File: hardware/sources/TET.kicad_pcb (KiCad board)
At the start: 4 copper layers, 90.2 x 95.9 mm, 97 parts, among them J1 SWD, M1 MountingHole, M2 MountingHole, M3 MountingHole, M4 MountingHole, U1 TCAN330GDCNR, U10 TLV75533PDBVR, U11 SMA_1, U12 W25Q128JVSIQTR, U13 W25Q128JVSIQTR, U14 E80-900M2213S, U15 SMA_2, U16 W25Q128JVSIQTR, U17 TMP112AIDRLR, U18 INA226AQDGSRQ1, U19 TMP112AIDRLR, U2 8 MHz, U3 STM32L431RBT6TR, U4 TMP112AIDRLR, U6 5015, U7 5015, U8 INA226AQDGSRQ1, U9 TMP112AIDRLR

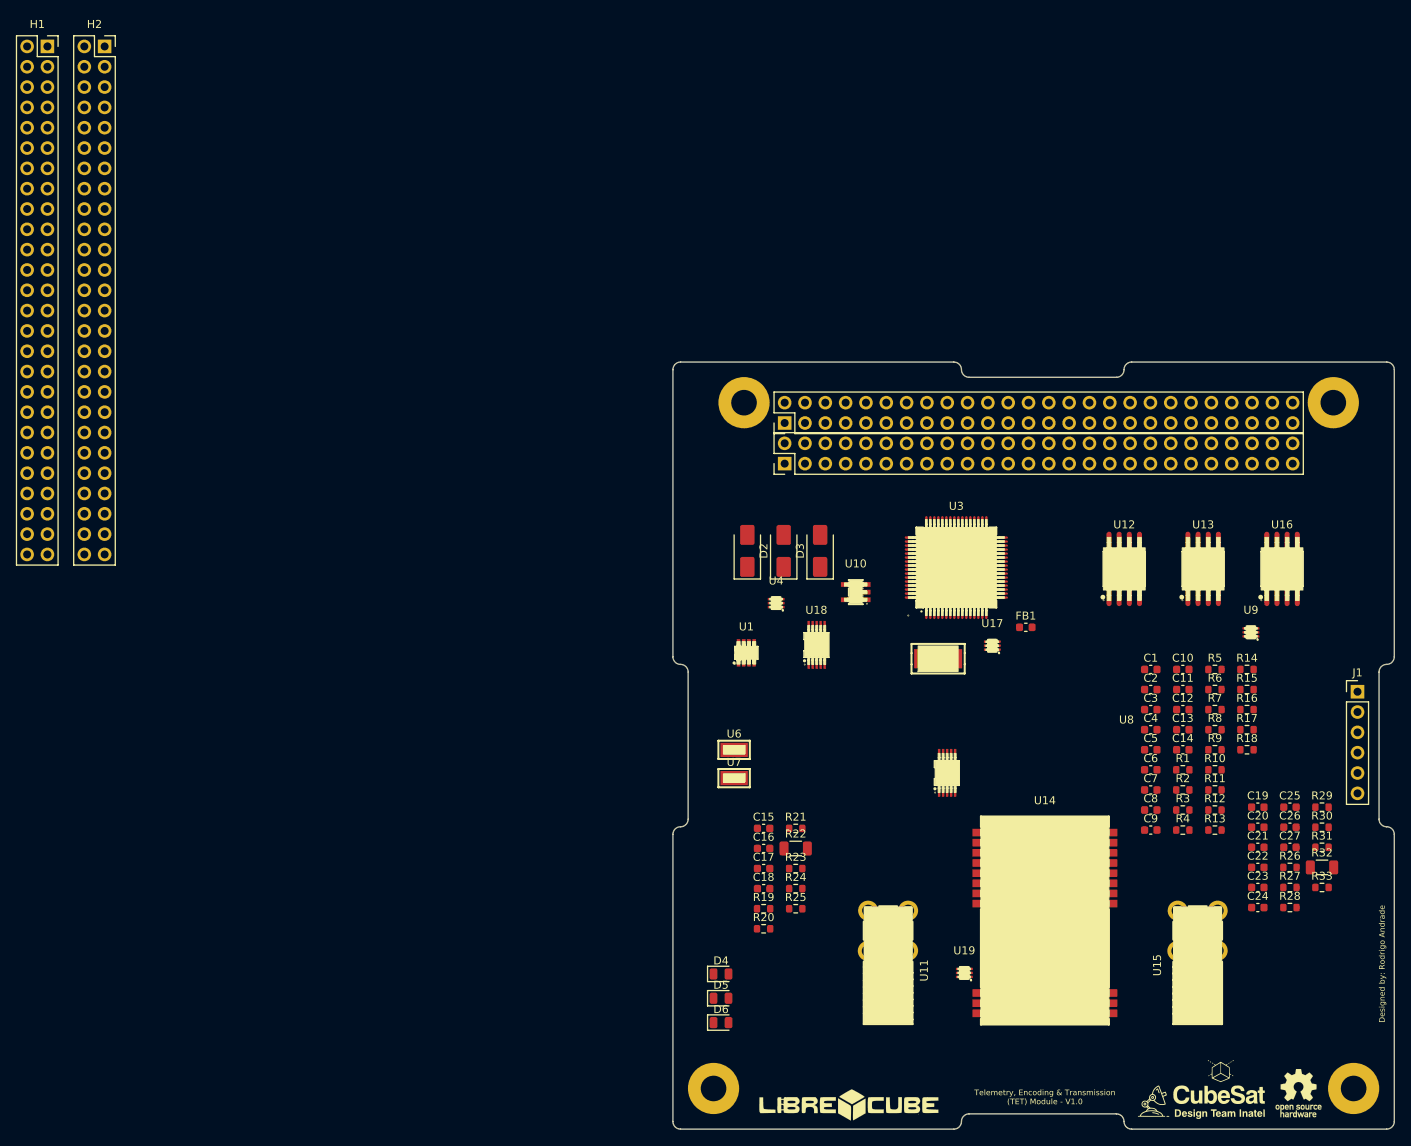
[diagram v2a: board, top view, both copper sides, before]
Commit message: hardware(schematic): fix Electrical Rules Check (ERC)
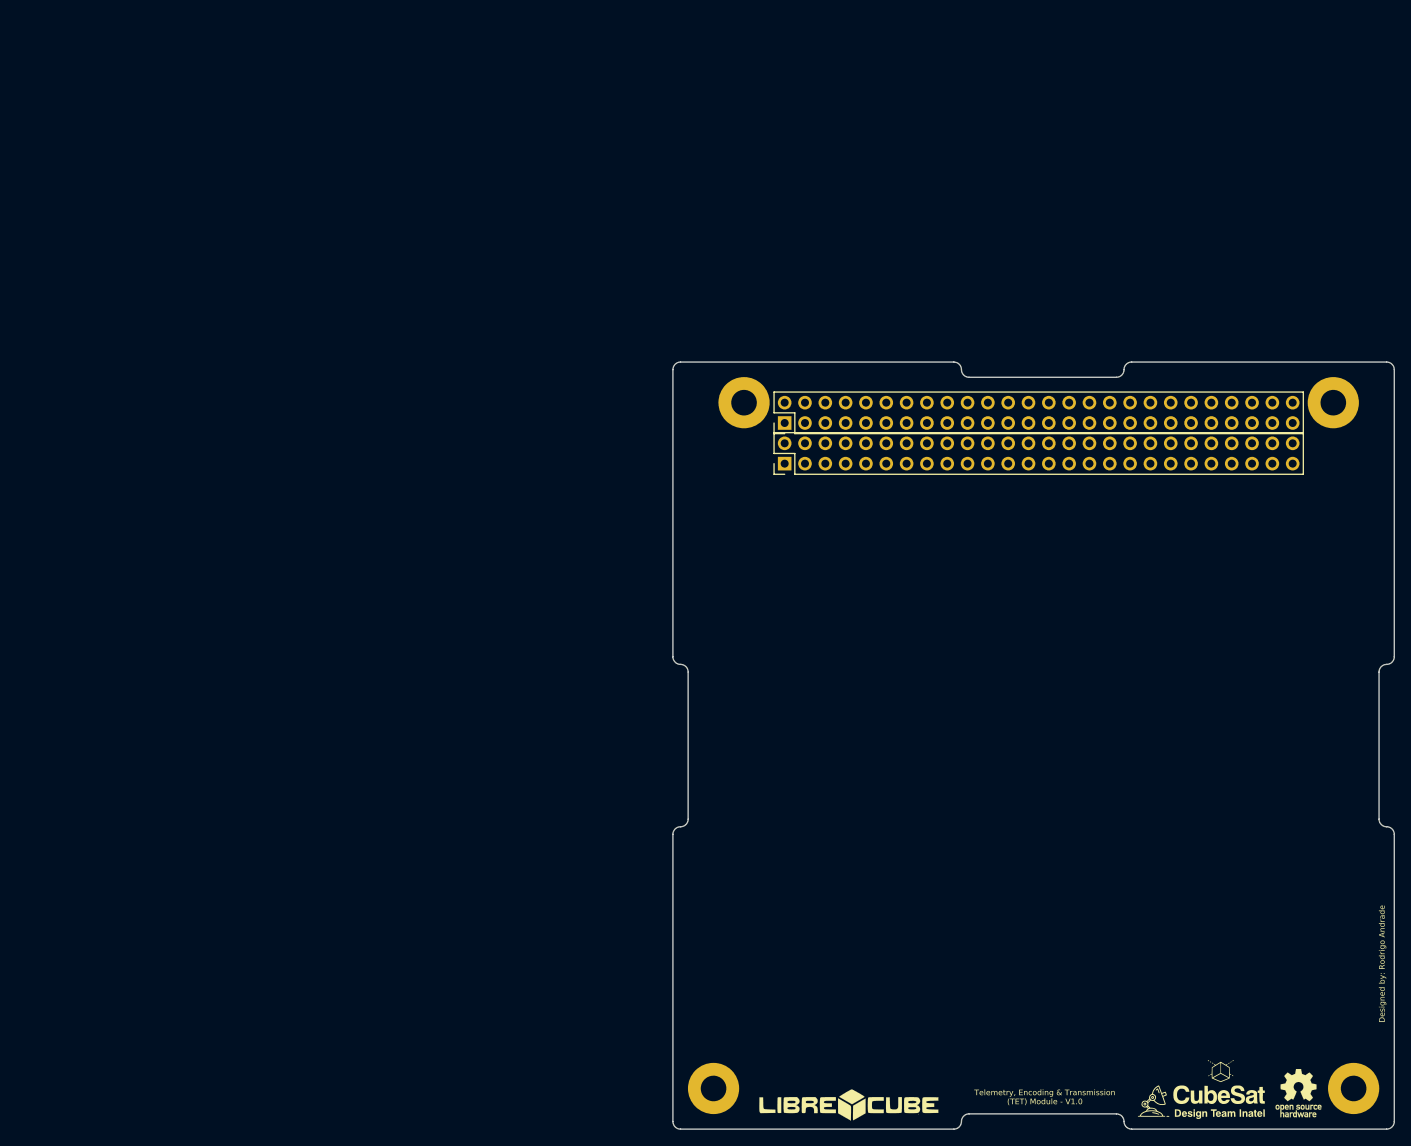
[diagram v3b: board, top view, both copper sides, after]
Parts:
- removed C1, C14, C15, C18, C19, C20, C24, C25, C26, C27: 0.1uF, Capacitor_SMD:C_0603_1608Metric
- removed C10, C22, C23, C3, C5, C6, C7, C9: 100nF, Capacitor_SMD:C_0603_1608Metric
- removed C11: 10nF, Capacitor_SMD:C_0603_1608Metric
- removed C12, C13: 1uF, Capacitor_SMD:C_0603_1608Metric
- removed C16, C17, C21: 22uF, Capacitor_SMD:C_0603_1608Metric
- removed C2, C4: 20pF, Capacitor_SMD:C_0603_1608Metric
- removed C8: 4.7 nF, Capacitor_SMD:C_0603_1608Metric
- removed D1, D2, D3: SS14, Diode_SMD:D_SMA
- removed D4: TX_LED, LED_SMD:LED_0805_2012Metric
- removed D5: RX_LED, LED_SMD:LED_0805_2012Metric
- removed D6: ON_LED, LED_SMD:LED_0805_2012Metric
- removed FB1: 120R, Inductor_SMD:L_0603_1608Metric
- removed the H1 at (4.37, 1.82)
- removed the H2 at (11.5, 1.82)
- removed J1: SWD, Connector_PinHeader_2.54mm:PinHeader_1x06_P2.54mm_Vertical
- removed R1, R15, R16, R18, R19, R2, R24, R26, R27, R28, R30, R31, R5: 10k, Resistor_SMD:R_0603_1608Metric
- removed R10, R11, R12, R13, R9: 33, Resistor_SMD:R_0603_1608Metric
- removed R14, R17, R23, R29, R33, R6, R7, R8: 4.7k, Resistor_SMD:R_0603_1608Metric
- removed R20: 200, Resistor_SMD:R_0603_1608Metric
- removed R21: 100, Resistor_SMD:R_0603_1608Metric
- removed R22, R32: 0.1, Resistor_SMD:R_1206_3216Metric
- removed R25: 270, Resistor_SMD:R_0603_1608Metric
- removed R3, R4: 60, Resistor_SMD:R_0603_1608Metric
- removed U1: TCAN330GDCNR, TET-Footprints:SOT-23-8_L2.9-W1.6-P0.65-LS2.8-BL
- removed U10: TLV75533PDBVR, TET-Footprints:SOT-23-5_L3.0-W1.7-P0.95-LS2.8-BR
- removed U11: SMA_1, TET-Footprints:SMA-TH_SMA-KWE_C7498154
- removed U12, U13, U16: W25Q128JVSIQTR, TET-Footprints:SOIC-8_L5.3-W5.3-P1.27-LS8.0-BL
- removed U14: E80-900M2213S, TET-Footprints:WIFIM-SMD_22P-L26.0-W16.0-P1.27-TL
- removed U15: SMA_2, TET-Footprints:SMA-TH_SMA-KWE_C7498154
- removed U17, U19, U4, U9: TMP112AIDRLR, TET-Footprints:SOT-563_L1.6-W1.2-P0.50-LS1.6-BR
- removed U18, U8: INA226AQDGSRQ1, TET-Footprints:VSSOP-10_L3.0-W3.0-P0.50-LS4.9-BL
- removed U2: 8 MHz, TET-Footprints:CRYSTAL-SMD_L5.0-W3.2
- removed U3: STM32L431RBT6TR, TET-Footprints:LQFP-64_L10.0-W10.0-P0.50-LS12.0-BL
- removed U6, U7: 5015, TET-Footprints:TEST-SMD_L2.7-W1.0

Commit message: hardware(pcb_design): start PCB design
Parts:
- added C1: 0.1uF, Capacitor_SMD:C_0603_1608Metric, F.Cu at (233.0, 114.5)
- added C10: 100nF, Capacitor_SMD:C_0603_1608Metric, F.Cu at (237.0, 114.5)
- added C11: 10nF, Capacitor_SMD:C_0603_1608Metric, F.Cu at (237.0, 117.0)
- added C12: 1uF, Capacitor_SMD:C_0603_1608Metric, F.Cu at (237.0, 119.5)
- added C13: 1uF, Capacitor_SMD:C_0603_1608Metric, F.Cu at (237.0, 122.0)
- added C14: 0.1uF, Capacitor_SMD:C_0603_1608Metric, F.Cu at (237.0, 124.6)
- added C15: 0.1uF, Capacitor_SMD:C_0603_1608Metric, F.Cu at (222.9, 83.7)
- added C16: 22uF, Capacitor_SMD:C_0603_1608Metric, F.Cu at (222.9, 86.2)
- added C17: 22uF, Capacitor_SMD:C_0603_1608Metric, F.Cu at (222.9, 88.7)
- added C18: 0.1uF, Capacitor_SMD:C_0603_1608Metric, F.Cu at (222.9, 91.2)
- added C19: 0.1uF, Capacitor_SMD:C_0603_1608Metric, F.Cu at (252.6, 97.5)
- added C2: 20pF, Capacitor_SMD:C_0603_1608Metric, F.Cu at (233.0, 117.0)
- added C20: 0.1uF, Capacitor_SMD:C_0603_1608Metric, F.Cu at (252.6, 100.0)
- added C21: 22uF, Capacitor_SMD:C_0603_1608Metric, F.Cu at (252.6, 102.5)
- added C22: 100nF, Capacitor_SMD:C_0603_1608Metric, F.Cu at (252.6, 105.0)
- added C23: 100nF, Capacitor_SMD:C_0603_1608Metric, F.Cu at (252.6, 107.5)
- added C24: 0.1uF, Capacitor_SMD:C_0603_1608Metric, F.Cu at (252.6, 110.0)
- added C25: 0.1uF, Capacitor_SMD:C_0603_1608Metric, F.Cu at (256.6, 97.5)
- added C26: 0.1uF, Capacitor_SMD:C_0603_1608Metric, F.Cu at (256.6, 100.0)
- added C27: 0.1uF, Capacitor_SMD:C_0603_1608Metric, F.Cu at (256.6, 102.5)
- added C3: 100nF, Capacitor_SMD:C_0603_1608Metric, F.Cu at (233.0, 119.5)
- added C4: 20pF, Capacitor_SMD:C_0603_1608Metric, F.Cu at (233.0, 122.0)
- added C5: 100nF, Capacitor_SMD:C_0603_1608Metric, F.Cu at (233.0, 124.6)
- added C6: 100nF, Capacitor_SMD:C_0603_1608Metric, F.Cu at (233.0, 127.1)
- added C7: 100nF, Capacitor_SMD:C_0603_1608Metric, F.Cu at (233.0, 129.6)
- added C8: 4.7 nF, Capacitor_SMD:C_0603_1608Metric, F.Cu at (93.8, 83.8)
- added C9: 100nF, Capacitor_SMD:C_0603_1608Metric, F.Cu at (194.7, 129.0)
- added D1: SS14, Diode_SMD:D_SMA, F.Cu at (160.0, 65.6)
- added D2: SS14, Diode_SMD:D_SMA, F.Cu at (143.3, 65.6)
- added D3: SS14, Diode_SMD:D_SMA, F.Cu at (151.7, 65.6)
- added D4: TX_LED, LED_SMD:LED_0805_2012Metric, F.Cu at (223.1, 96.5)
- added D5: RX_LED, LED_SMD:LED_0805_2012Metric, F.Cu at (223.1, 99.6)
- added D6: ON_LED, LED_SMD:LED_0805_2012Metric, F.Cu at (223.1, 102.6)
- added FB1: 120R, Inductor_SMD:L_0603_1608Metric, F.Cu at (237.0, 127.1)
- added J1: SWD, Connector_PinHeader_2.54mm:PinHeader_1x06_P2.54mm_Vertical, F.Cu at (89.0, 82.9)
- added R1: 10k, Resistor_SMD:R_0603_1608Metric, F.Cu at (237.0, 129.6)
- added R10: 33, Resistor_SMD:R_0603_1608Metric, F.Cu at (113.2, 78.4)
- added R11: 33, Resistor_SMD:R_0603_1608Metric, F.Cu at (113.2, 75.4)
- added R12: 33, Resistor_SMD:R_0603_1608Metric, F.Cu at (113.2, 72.4)
- added R13: 33, Resistor_SMD:R_0603_1608Metric, F.Cu at (113.2, 69.4)
- added R14: 4.7k, Resistor_SMD:R_0603_1608Metric, F.Cu at (245.0, 117.0)
- added R15: 10k, Resistor_SMD:R_0603_1608Metric, F.Cu at (245.0, 119.5)
- added R16: 10k, Resistor_SMD:R_0603_1608Metric, F.Cu at (245.0, 122.0)
- added R17: 4.7k, Resistor_SMD:R_0603_1608Metric, F.Cu at (245.0, 124.6)
- added R18: 10k, Resistor_SMD:R_0603_1608Metric, F.Cu at (245.0, 127.1)
- added R19: 10k, Resistor_SMD:R_0603_1608Metric, F.Cu at (222.9, 93.8)
- added R2: 10k, Resistor_SMD:R_0603_1608Metric, F.Cu at (237.0, 132.1)
- added R20: 200, Resistor_SMD:R_0603_1608Metric, F.Cu at (226.9, 83.7)
- added R21: 100, Resistor_SMD:R_0603_1608Metric, F.Cu at (226.9, 86.2)
- added R22: 0.1, Resistor_SMD:R_1206_3216Metric, F.Cu at (151.7, 76.5)
- added R23: 4.7k, Resistor_SMD:R_0603_1608Metric, F.Cu at (226.9, 88.7)
- added R24: 10k, Resistor_SMD:R_0603_1608Metric, F.Cu at (226.9, 91.2)
- added R25: 270, Resistor_SMD:R_0603_1608Metric, F.Cu at (226.9, 93.8)
- added R26: 10k, Resistor_SMD:R_0603_1608Metric, F.Cu at (256.6, 105.0)
- added R27: 10k, Resistor_SMD:R_0603_1608Metric, F.Cu at (256.6, 107.5)
- added R28: 10k, Resistor_SMD:R_0603_1608Metric, F.Cu at (256.6, 110.0)
- added R29: 4.7k, Resistor_SMD:R_0603_1608Metric, F.Cu at (113.2, 81.4)
- added R3: 60, Resistor_SMD:R_0603_1608Metric, F.Cu at (93.8, 86.8)
- added R30: 10k, Resistor_SMD:R_0603_1608Metric, F.Cu at (260.6, 100.0)
- added R31: 10k, Resistor_SMD:R_0603_1608Metric, F.Cu at (260.6, 102.5)
- added R32: 0.1, Resistor_SMD:R_1206_3216Metric, F.Cu at (233.8, 108.0)
- added R33: 4.7k, Resistor_SMD:R_0603_1608Metric, F.Cu at (113.2, 82.9)
- added R4: 60, Resistor_SMD:R_0603_1608Metric, F.Cu at (93.8, 85.3)
- added R5: 10k, Resistor_SMD:R_0603_1608Metric, F.Cu at (241.0, 117.0)
- added R6: 4.7k, Resistor_SMD:R_0603_1608Metric, F.Cu at (241.0, 119.5)
- added R7: 4.7k, Resistor_SMD:R_0603_1608Metric, F.Cu at (241.0, 122.0)
- added R8: 4.7k, Resistor_SMD:R_0603_1608Metric, F.Cu at (113.2, 66.4)
- added R9: 33, Resistor_SMD:R_0603_1608Metric, F.Cu at (113.2, 84.4)
- added U1: TCAN330GDCNR, TET-Footprints:SOT-23-8_L2.9-W1.6-P0.65-LS2.8-BL, F.Cu at (97.9, 85.8)
- added U10: TLV75533PDBVR, TET-Footprints:SOT-23-5_L3.0-W1.7-P0.95-LS2.8-BR, F.Cu at (160.0, 76.5)
- added U11: SMA_1, TET-Footprints:SMA-TH_SMA-KWE_C7498154, F.Cu at (94.3, 122.5)
- added U12: W25Q128JVSIQTR, TET-Footprints:SOIC-8_L5.3-W5.3-P1.27-LS8.0-BL, F.Cu at (129.0, 62.5)
- added U13: W25Q128JVSIQTR, TET-Footprints:SOIC-8_L5.3-W5.3-P1.27-LS8.0-BL, F.Cu at (128.0, 82.1)
- added U14: E80-900M2213S, TET-Footprints:WIFIM-SMD_22P-L26.0-W16.0-P1.27-TL, F.Cu at (129.0, 112.5)
- added U15: SMA_2, TET-Footprints:SMA-TH_SMA-KWE_C7498154, F.Cu at (160.9, 122.5)
- added U16: W25Q128JVSIQTR, TET-Footprints:SOIC-8_L5.3-W5.3-P1.27-LS8.0-BL, F.Cu at (120.0, 62.5)
- added U17: TMP112AIDRLR, TET-Footprints:SOT-563_L1.6-W1.2-P0.50-LS1.6-BR, F.Cu at (59.7, 81.0)
- added U18: INA226AQDGSRQ1, TET-Footprints:VSSOP-10_L3.0-W3.0-P0.50-LS4.9-BL, F.Cu at (218.5, 26.9)
- added U19: TMP112AIDRLR, TET-Footprints:SOT-563_L1.6-W1.2-P0.50-LS1.6-BR, F.Cu at (66.0, 51.5)
- added U2: 8 MHz, TET-Footprints:CRYSTAL-SMD_L5.0-W3.2, F.Cu at (128.5, 90.5)
- added U3: STM32L431RBT6TR, TET-Footprints:LQFP-64_L10.0-W10.0-P0.50-LS12.0-BL, F.Cu at (103.5, 73.5)
- added U4: TMP112AIDRLR, TET-Footprints:SOT-563_L1.6-W1.2-P0.50-LS1.6-BR, F.Cu at (257.4, 119.6)
- added U6: 5015, TET-Footprints:TEST-SMD_L2.7-W1.0, F.Cu at (208.5, 105.0)
- added U7: 5015, TET-Footprints:TEST-SMD_L2.7-W1.0, F.Cu at (213.0, 109.5)
- added U8: INA226AQDGSRQ1, TET-Footprints:VSSOP-10_L3.0-W3.0-P0.50-LS4.9-BL, F.Cu at (143.3, 76.6)
- added U9: TMP112AIDRLR, TET-Footprints:SOT-563_L1.6-W1.2-P0.50-LS1.6-BR, F.Cu at (227.1, 122.9)
- H1, H2: footprint Connector_PinHeader_2.54mm:PinHeader_2x26_P2.54mm_Vertical -> TET-Footprints:PinHeader_2x26_P2.54mm_Vertical
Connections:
- H1 pad 13: /UART_C_TX -> unconnected-(H1-Pin_13-Pad13)
- H1 pad 15: /UART_C_RX -> unconnected-(H1-Pin_15-Pad15)
- H1 pad 2: /CAN_B_L -> unconnected-(H1-Pin_2-Pad2)
- H1 pad 22: /UART_D_TX -> unconnected-(H1-Pin_22-Pad22)
- H1 pad 24: /UART_D_RX -> unconnected-(H1-Pin_24-Pad24)
- H1 pad 25: /5V_PERM -> unconnected-(H1-Pin_25-Pad25)
- H1 pad 26: /5V_PERM -> unconnected-(H1-Pin_26-Pad26)
- H1 pad 31: /CHARGE -> unconnected-(H1-Pin_31-Pad31)
- H1 pad 32: /CHARGE -> unconnected-(H1-Pin_32-Pad32)
- H1 pad 38: /UART_E_TX -> unconnected-(H1-Pin_38-Pad38)
- H1 pad 4: /CAN_B_H -> unconnected-(H1-Pin_4-Pad4)
- H1 pad 40: /UART_E_RX -> unconnected-(H1-Pin_40-Pad40)
- H1 pad 42: /UART_F_TX -> unconnected-(H1-Pin_42-Pad42)
- H1 pad 44: /UART_F_RX -> unconnected-(H1-Pin_44-Pad44)
- H1 pad 45: /ENA_PWR_1 -> unconnected-(H1-Pin_45-Pad45)
- H1 pad 46: /PWR_1 -> unconnected-(H1-Pin_46-Pad46)
- H1 pad 47: /ENA_PWR_2 -> unconnected-(H1-Pin_47-Pad47)
- H1 pad 48: /PWR_2 -> unconnected-(H1-Pin_48-Pad48)
- H1 pad 49: /ENA_PWR_3 -> unconnected-(H1-Pin_49-Pad49)
- H1 pad 50: /PWR_3 -> unconnected-(H1-Pin_50-Pad50)
- H1 pad 51: /ENA_PWR_4 -> unconnected-(H1-Pin_51-Pad51)
- H1 pad 52: /PWR_4 -> /Power_Supply/PWR_4
- H2 pad 1: /ENA_PWR_9 -> unconnected-(H2-Pin_1-Pad1)
- H2 pad 10: /PWR_13 -> unconnected-(H2-Pin_10-Pad10)
- H2 pad 11: /ENA_PWR_14 -> unconnected-(H2-Pin_11-Pad11)
- H2 pad 12: /PWR_14 -> unconnected-(H2-Pin_12-Pad12)
- H2 pad 13: /ENA_PWR_15 -> unconnected-(H2-Pin_13-Pad13)
- H2 pad 14: /PWR_15 -> unconnected-(H2-Pin_14-Pad14)
- H2 pad 15: /ENA_PWR_16 -> unconnected-(H2-Pin_15-Pad15)
- H2 pad 16: /PWR_16 -> unconnected-(H2-Pin_16-Pad16)
- H2 pad 17: /ENA_PWR_17 -> unconnected-(H2-Pin_17-Pad17)
- H2 pad 18: /PWR_17 -> unconnected-(H2-Pin_18-Pad18)
- H2 pad 19: /ENA_PWR_18 -> unconnected-(H2-Pin_19-Pad19)
- H2 pad 2: /PWR_9 -> unconnected-(H2-Pin_2-Pad2)
- H2 pad 20: /PWR_18 -> unconnected-(H2-Pin_20-Pad20)
- H2 pad 21: /ENA_PWR_19 -> unconnected-(H2-Pin_21-Pad21)
- H2 pad 22: /PWR_19 -> unconnected-(H2-Pin_22-Pad22)
- H2 pad 23: /ENA_PWR_20 -> unconnected-(H2-Pin_23-Pad23)
- H2 pad 24: /PWR_20 -> unconnected-(H2-Pin_24-Pad24)
- H2 pad 25: /5V_PERM -> unconnected-(H2-Pin_25-Pad25)
- H2 pad 26: /5V_PERM -> unconnected-(H2-Pin_26-Pad26)
- H2 pad 3: /ENA_PWR_10 -> unconnected-(H2-Pin_3-Pad3)
- H2 pad 33: /ENA_PWR_5 -> unconnected-(H2-Pin_33-Pad33)
- H2 pad 34: /PWR_5 -> /Power_Supply/PWR_5
- H2 pad 35: /ENA_PWR_6 -> unconnected-(H2-Pin_35-Pad35)
- H2 pad 36: /PWR_6 -> /Power_Supply/PWR_6
- H2 pad 37: /ENA_PWR_7 -> unconnected-(H2-Pin_37-Pad37)
- H2 pad 38: /PWR_7 -> unconnected-(H2-Pin_38-Pad38)
- H2 pad 39: /ENA_PWR_8 -> unconnected-(H2-Pin_39-Pad39)
- H2 pad 4: /PWR_10 -> unconnected-(H2-Pin_4-Pad4)
- H2 pad 40: /PWR_8 -> unconnected-(H2-Pin_40-Pad40)
- H2 pad 45: /BATT -> unconnected-(H2-Pin_45-Pad45)
- H2 pad 46: /BATT -> unconnected-(H2-Pin_46-Pad46)
- H2 pad 49: /RBF_A -> unconnected-(H2-Pin_49-Pad49)
- H2 pad 5: /ENA_PWR_11 -> unconnected-(H2-Pin_5-Pad5)
- H2 pad 50: /RBF_B -> unconnected-(H2-Pin_50-Pad50)
- H2 pad 51: /DS_A -> unconnected-(H2-Pin_51-Pad51)
- H2 pad 52: /DS_B -> unconnected-(H2-Pin_52-Pad52)
- H2 pad 6: /PWR_11 -> unconnected-(H2-Pin_6-Pad6)
- H2 pad 7: /ENA_PWR_12 -> unconnected-(H2-Pin_7-Pad7)
- H2 pad 8: /PWR_12 -> unconnected-(H2-Pin_8-Pad8)
- H2 pad 9: /ENA_PWR_13 -> unconnected-(H2-Pin_9-Pad9)
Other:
- board text removed: "Designed by: Rodrigo Andrade"

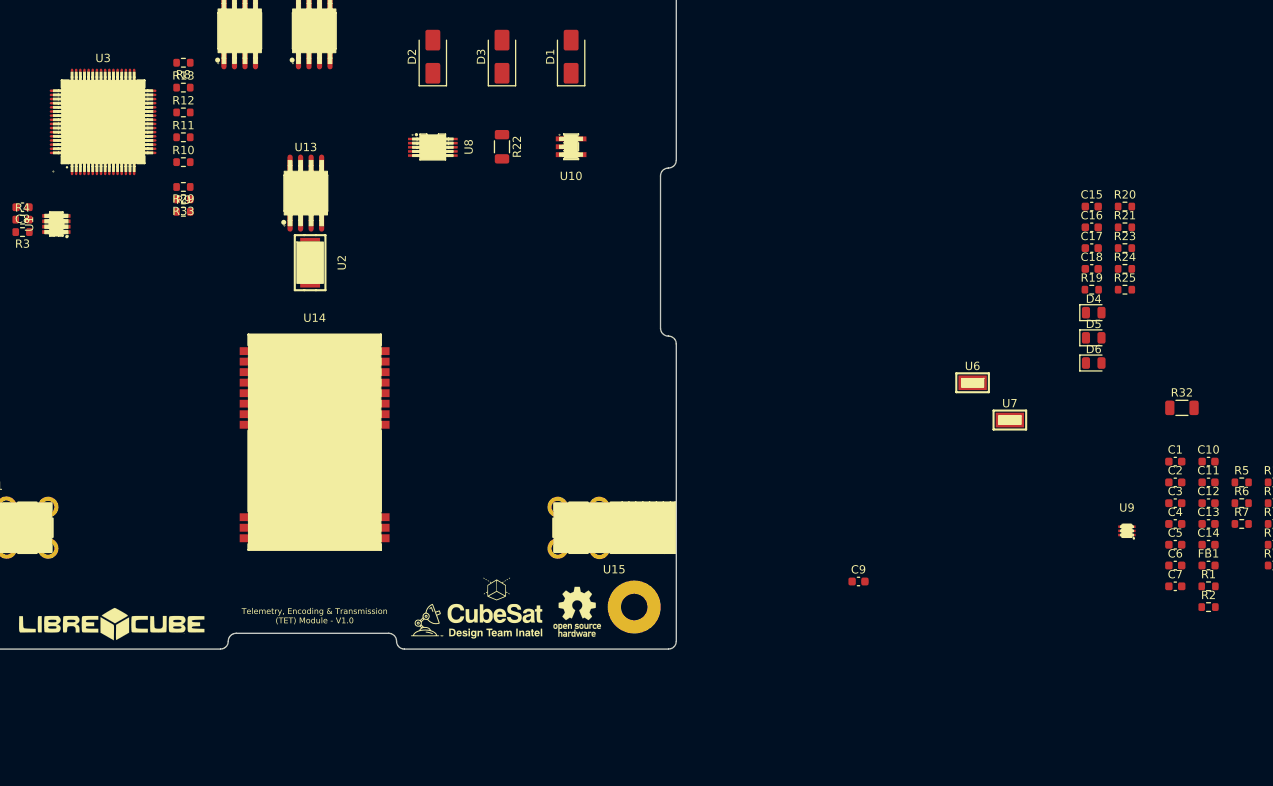
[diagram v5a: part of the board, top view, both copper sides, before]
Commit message: hardware(schematic): add bulk capacitor on STM32L4 #5
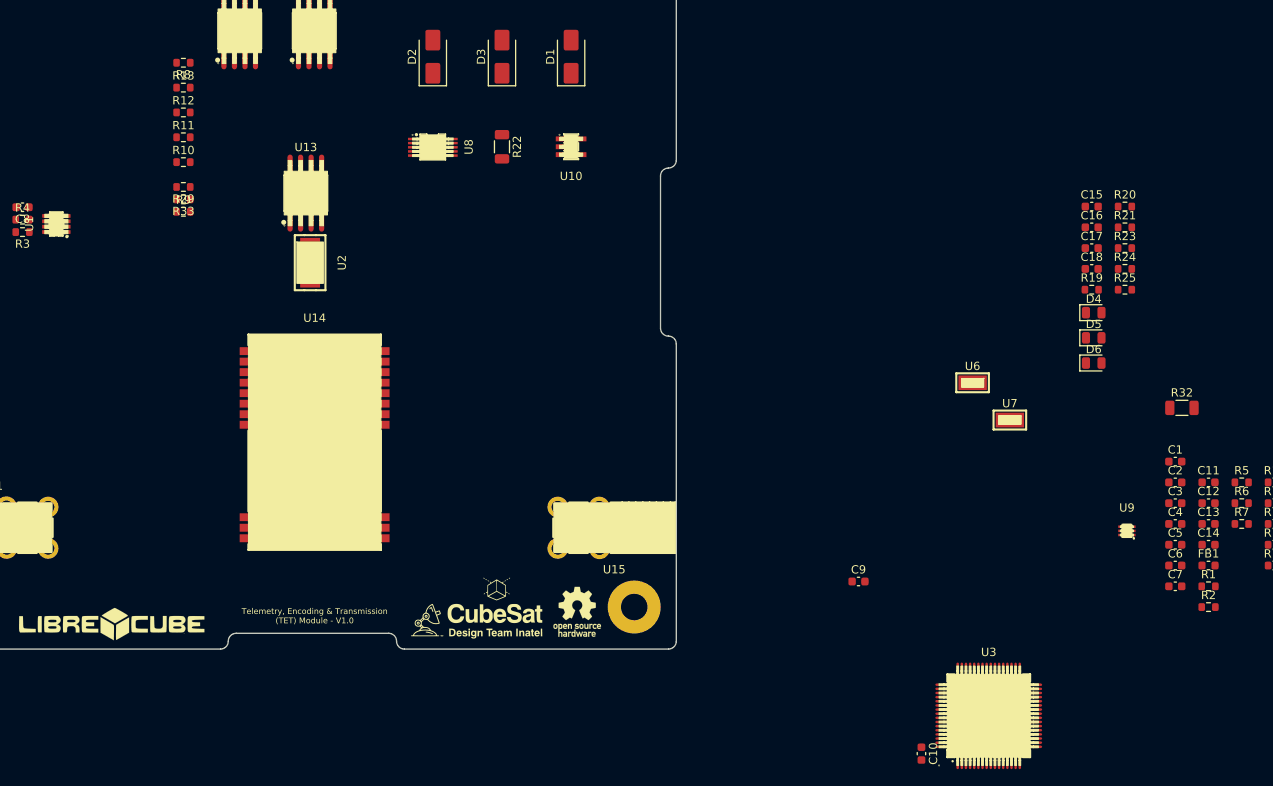
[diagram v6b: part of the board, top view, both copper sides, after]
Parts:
- moved U3 128.8 mm to (210.4, 145.2)
- moved C10 49.5 mm to (202.3, 149.8), turned to -90 degrees

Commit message: feat(schematic): fix double pull-up resistor for LR_BUSY
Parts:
- removed R2: 10k, Resistor_SMD:R_0603_1608Metric
- added C28: 10uF, Capacitor_SMD:C_0603_1608Metric, F.Cu at (27.6, 20.7)
- C19, C20, C24, C25: value 0.1uF -> 100nF
- moved R14 231.1 mm to (27.7, 38.4)
- moved R15 231.1 mm to (27.7, 40.9)
- moved R16 231.1 mm to (27.7, 43.4)
- moved R17 231.1 mm to (27.7, 45.9)
- moved R18 231.1 mm to (27.7, 48.4)
- moved R7 230.7 mm to (27.7, 34.2)
- moved C3 226.5 mm to (7.02, 103.9), turned to 180 degrees
- moved C11 223.8 mm to (13.6, 103.9), turned to 180 degrees
- moved C2 223.1 mm to (10.2, 106.0)
- moved C4 220.0 mm to (13.6, 106.0)
- moved R5 218.3 mm to (27.2, 72.9)
- moved C12 218.2 mm to (19.3, 104.7), turned to -90 degrees
- moved FB1 218.1 mm to (20.3, 102.0)
- moved C7 216.7 mm to (19.5, 92.5), turned to -90 degrees
- moved C13 216.4 mm to (21.3, 104.7), turned to -90 degrees
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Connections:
- R27 pad 2: /FLASH3_CS -> /FLASH2_CS
- R30 pad 2: /FLASH2_CS -> /FLASH3_CS
- U13 pad 1: /FLASH3_CS -> /FLASH2_CS
- U16 pad 1: /FLASH2_CS -> /FLASH3_CS

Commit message: hardware(pcb_design): components Micro-Placement
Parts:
- R3, R4: footprint Resistor_SMD:R_0603_1608Metric -> Resistor_SMD:R_0603_1608Metric_Pad0.98x0.95mm_HandSolder
- moved C1 135.8 mm to (100.0, 86.6), turned to 90 degrees
- moved D6 117.7 mm to (87.8, 59.1), turned to -90 degrees
- moved R25 117.1 mm to (90.5, 59.0), turned to 90 degrees
- moved C26 110.5 mm to (146.3, 93.1), turned to -90 degrees
- moved D4 107.3 mm to (87.8, 67.1), turned to -90 degrees
- moved R20 106.6 mm to (90.5, 67.0), turned to 90 degrees
- moved R23 98.8 mm to (146.6, 80.6)
- moved C18 98.8 mm to (140.6, 81.7)
- moved U9 98.8 mm to (143.3, 81.9)
- moved D5 97.3 mm to (87.8, 75.1), turned to -90 degrees
- moved R21 96.6 mm to (90.5, 75.0), turned to 90 degrees
- moved C15 95.0 mm to (156.6, 75.4), turned to -90 degrees
- moved R32 85.8 mm to (149.7, 90.6), turned to -90 degrees
- moved C27 85.0 mm to (112.0, 100.4)
- moved R33 85.0 mm to (118.0, 99.8)
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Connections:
- C16 pad 1: /Power_Supply/POWER_SENSE- -> +5V
- C21 pad 1: /RF_Transceiver/RF_SENSE+ -> +3.3V
- C22 pad 1: /RF_Transceiver/RF_SENSE+ -> +3.3V
- R22 pad 2: /Power_Supply/POWER_SENSE- -> +5V
- R24 pad 1: /Power_Supply/POWER_SENSE- -> +5V
- R28 pad 1: /RF_Transceiver/RF_SENSE+ -> +3.3V
- R32 pad 1: /RF_Transceiver/RF_SENSE+ -> +3.3V
- U10 pad 1: /Power_Supply/POWER_SENSE- -> +5V
- U14 pad 25: /RF_Transceiver/RF_SENSE+ -> +3.3V
- U18 pad 10: /RF_Transceiver/RF_SENSE+ -> +3.3V
- U8 pad 8: /Power_Supply/POWER_SENSE- -> +5V
- U8 pad 9: /Power_Supply/POWER_SENSE- -> +5V
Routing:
- net +5V: track 0.00 -> 36.1 mm
- net /RF_Transceiver/ANT_2.4: track 0.00 -> 26.7 mm
- net /RF_Transceiver/ANT_915: track 0.00 -> 23.9 mm
- net +3.3V: track 0.00 -> 7.76 mm
- net Net-(U10-EN): track 0.00 -> 3.80 mm
